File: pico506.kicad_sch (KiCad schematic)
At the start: 62 parts, among them J1 ST-506 CONTROL, J2 ST-506 DATA, J3 AMP 350211-1, J4 DRIVE SELECT, J5 UART, J6 SERVO GATE 3V3, J7 FRONT LED, Q1 2N3904, SW1 RESET, U1 Raspberry Pi Pico, U2 74LS05, U3 74LS05, U4 7438, U5 7438, U6 AM26LS31CN, U7 MC3486N

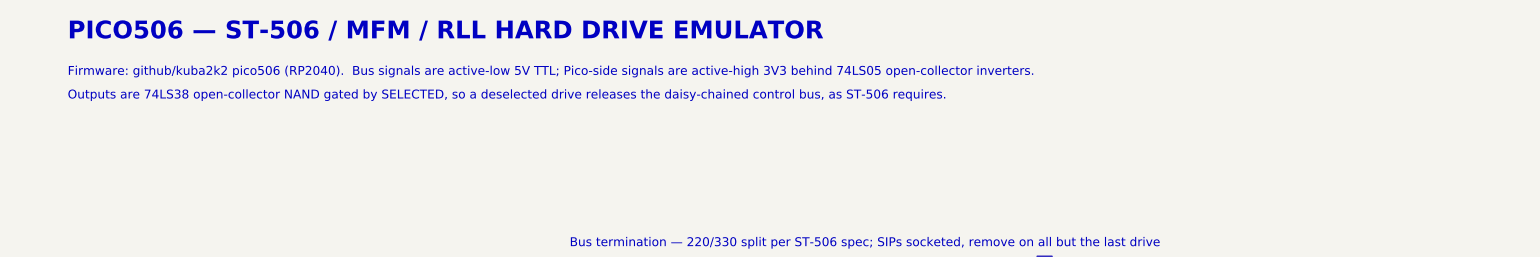
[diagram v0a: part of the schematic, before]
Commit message: Point silkscreen at this repo, credit upstream firmware
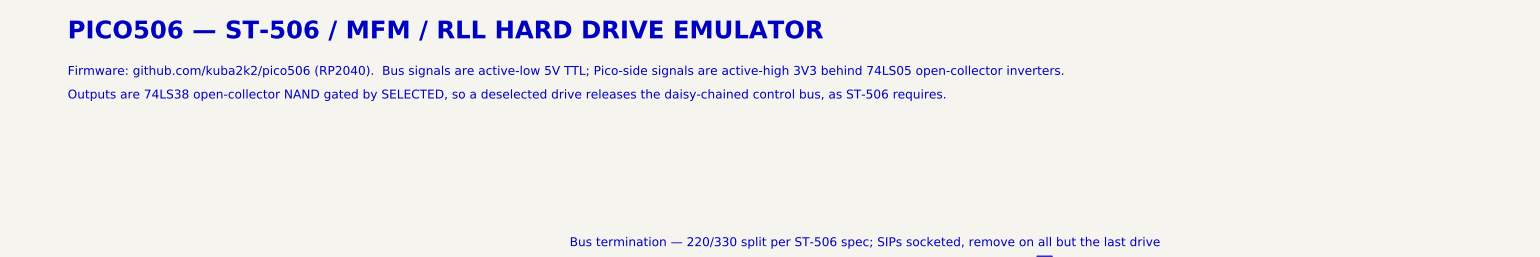
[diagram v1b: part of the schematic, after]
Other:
- note added: "Firmware: github.com/kuba2k2/pico506 (RP2040). Bus signals are active-low 5V TTL; Pico-side signals are active-high 3V3 behind 74LS05 open-collector inverters."
- note removed: "Firmware: github/kuba2k2 pico506 (RP2040). Bus signals are active-low 5V TTL; Pico-side signals are active-high 3V3 behind 74LS05 open-collector inverters."
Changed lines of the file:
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@@
     (rev "1.0")
     (comment 1 "Drop-in replacement PCB for classic 5.25-inch MFM drives")
+    (comment 2 "Board: github.com/hmerrett/pico506-pcb")
+    (comment 3 "Firmware: github.com/kuba2k2/pico506 (c) 2025 Kuba Szczodrzynski")
+    (comment 4 "Licensed GPL-3.0-or-later. Design files: see Board above.")
   )
   (text "PICO506 — ST-506 / MFM / RLL HARD DRIVE EMULATOR"
@@
     (effects (font (size 3 3) (bold yes)) (justify left bottom))
   )
-  (text "Firmware: github/kuba2k2 pico506 (RP2040).  Bus signals are active-low 5V TTL; Pico-side signals are active-high 3V3 behind 74LS05 open-collector inverters."
+  (text "Firmware: github.com/kuba2k2/pico506 (RP2040).  Bus signals are active-low 5V TTL; Pico-side signals are active-high 3V3 behind 74LS05 open-collector inverters."
     (exclude_from_sim no)
     (at 20 26 0)
